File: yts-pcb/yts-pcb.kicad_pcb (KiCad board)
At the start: 2 copper layers, 62 parts, among them J1 B+, J2 B-, SW1 ON/OFF, SW10 MX, SW11 MX, SW12 MX, SW13 MX, SW14 MX, SW15 MX, SW16 MX, SW17 MX, SW18 MX, SW19 MX, SW2 MX, SW20 MX, SW21 MX, SW22 MX, SW23 MX, SW24 MX, SW25 MX, SW26 MX, SW27 MX, SW28 MX, SW29 RotaryEncoder_Switch, SW3 MX, SW30 RotaryEncoder_Switch, SW4 MX, SW5 MX, SW6 MX, SW7 MX, SW8 MX, SW9 MX, U1 Nice!Nano

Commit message: finish pcb layout
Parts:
- D1, D10, D11, D12, D13, D14, D15, D16, D17, D18, D19, D2, D20, D21, D22, D23, D24, D25, D26, D27, D28, D29, D3, D4, D5, D6, D7, D8, D9: moved to B.Cu
- moved SW22 148.3 mm to (183.0, 61.4)
- moved SW26 147.5 mm to (202.0, 61.4)
- moved SW18 132.1 mm to (164.0, 42.4)
- moved SW25 129.3 mm to (202.0, 42.4)
- moved D24 125.6 mm to (209.0, 47.0), turned to 90 degrees
- moved SW27 122.1 mm to (202.0, 99.4)
- moved D1 111.9 mm to (57.0, 47.4), turned to 90 degrees
- moved SW24 107.5 mm to (183.0, 99.4)
- moved SW3 104.9 mm to (50.0, 61.4)
- moved D29 102.9 mm to (237.4, 107.5)
- moved D5 102.5 mm to (76.0, 47.4), turned to 90 degrees
- moved D7 99.1 mm to (76.0, 85.5), turned to 90 degrees
- moved D4 98.8 mm to (57.0, 104.5), turned to 90 degrees
- moved D3 97.9 mm to (57.0, 85.5), turned to 90 degrees
- moved SW1 88.8 mm to (143.0, 39.0), turned to 180 degrees
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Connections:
- D28 pad 2: row1 -> row2
- SW28 pad 2: col7 -> col4
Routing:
- net row2: track 0.00 -> 232.7 mm
- net row3: track 0.00 -> 197.1 mm, vias 0 -> 2
- net row0: track 0.00 -> 193.3 mm, vias 0 -> 1
- net GND: track 0.00 -> 178.6 mm, vias 0 -> 2
- net col0: track 0.00 -> 176.9 mm
- net col7: track 0.00 -> 166.4 mm
- net row1: track 0.00 -> 161.0 mm, vias 0 -> 1
- net col1: track 0.00 -> 154.8 mm
- net enc2: track 0.00 -> 135.0 mm, vias 0 -> 1
- net col2: track 0.00 -> 132.5 mm
- net enc3: track 0.00 -> 130.6 mm, vias 0 -> 3
- net col6: track 0.00 -> 126.1 mm
- net enc1: track 0.00 -> 118.4 mm, vias 0 -> 2
- net enc0: track 0.00 -> 117.4 mm
- net col4: track 0.00 -> 115.9 mm
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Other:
- board outline added: 210 x 78 mm

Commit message: update switchblade
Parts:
- moved D1 5.00 mm to (60.0, 51.4)
- moved D10 5.00 mm to (98.0, 70.5)
- moved D11 5.00 mm to (98.0, 89.5)
- moved D12 5.00 mm to (98.0, 108.5)
- moved D13 5.00 mm to (117.0, 51.0)
- moved D14 5.00 mm to (117.0, 70.5)
- moved D15 5.00 mm to (117.0, 89.5)
- moved D16 5.00 mm to (117.0, 108.5)
- moved D17 5.00 mm to (174.0, 51.0)
- moved D18 5.00 mm to (174.0, 70.5)
- moved D19 5.00 mm to (174.0, 108.5)
- moved D2 5.00 mm to (60.0, 70.6)
- moved D20 5.00 mm to (193.0, 51.0)
- moved D21 5.00 mm to (193.0, 70.5)
- moved D22 5.00 mm to (193.0, 89.5)
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
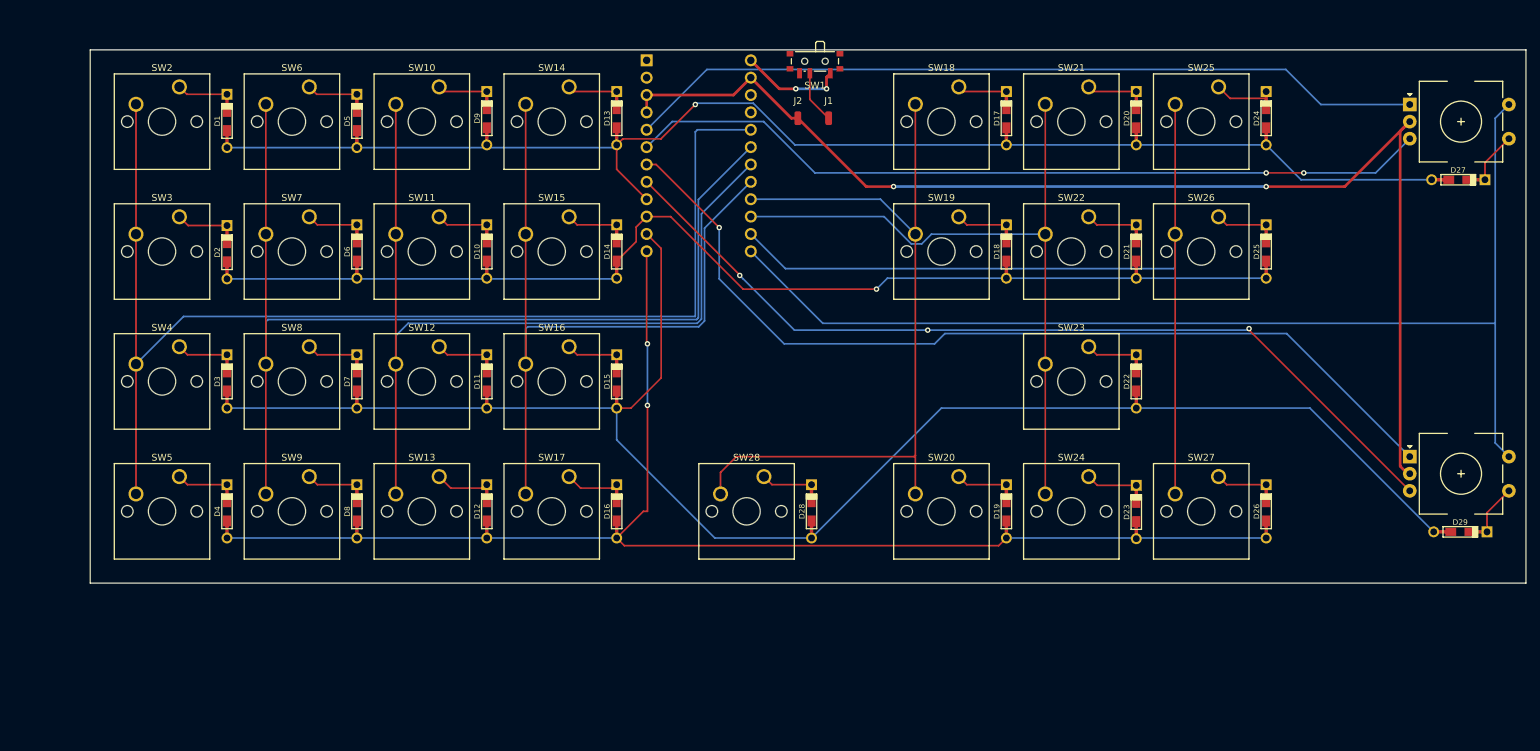
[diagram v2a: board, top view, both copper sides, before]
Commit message: update mx switches footprints to plate mount
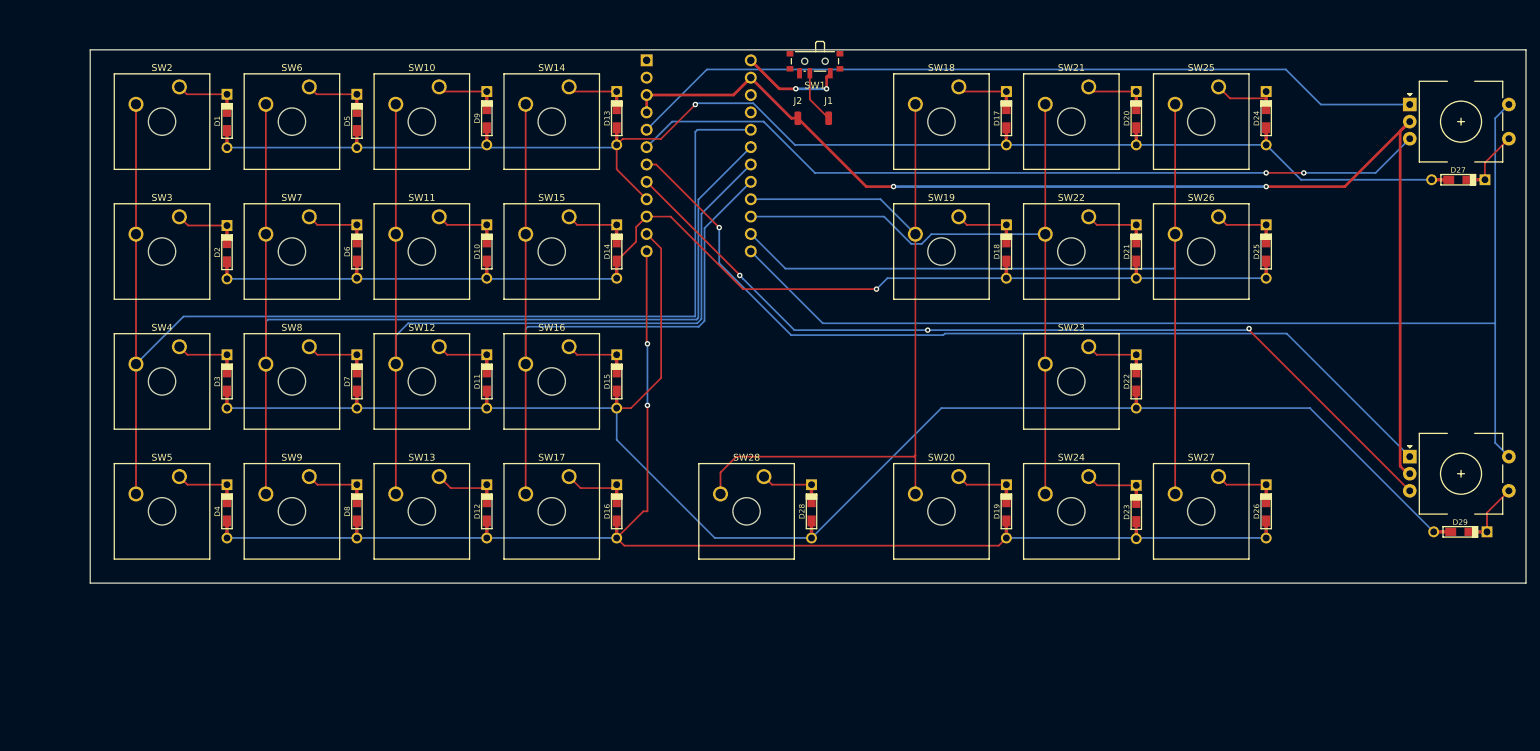
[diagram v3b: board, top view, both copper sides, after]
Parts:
- SW10, SW11, SW12, SW13, SW14, SW15, SW16, SW17, SW18, SW19, SW2, SW20, SW21, SW22, SW23, SW24, SW25, SW26, SW27, SW28, SW3, SW4, SW5, SW6, SW7, SW8, SW9: footprint Button_Switch_Keyboard:SW_Cherry_MX_1.00u_PCB -> Button_Switch_Keyboard:SW_Cherry_MX_1.00u_Plate
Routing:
- net enc2: track 135.0 -> 132.6 mm
